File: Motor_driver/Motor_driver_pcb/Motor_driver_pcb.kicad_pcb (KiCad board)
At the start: 2 copper layers, 89 parts, among them J1 USB_B, J10 Stepper AB, J11 Uni_stepper, J2 Power, J3 Servo 1, J4 Servo 2, J5 Encoder 1, J6 Encoder 2, J7 Stepper CD, J8 Motor 1, J9 Motor 2, Q1 Q_NPN_EBC, Q10 IRF9540N, Q11 IRF540N, Q12 Q_NPN_EBC, Q13 Q_NPN_EBC, Q14 IRF9540N, Q15 IRF540N, Q16 IRF9540N, Q17 IRF540N, Q18 Q_NPN_EBC, Q19 Q_NPN_EBC, Q2 IRF9540N, Q20 IRF9540N, Q21 IRF540N, Q22 IRF9540N, Q23 IRF540N, Q24 Q_NPN_EBC, Q3 IRF540N, Q4 IRF9540N, Q5 IRF540N, Q6 Q_NPN_EBC, Q7 Q_NPN_EBC, Q8 IRF9540N, Q9 IRF540N, U1 LM2596S_Module, U2 FT232RL, U3 STM32F103C8T6, U4 CD40106BE, U5 CD40106BE

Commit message: finish schema and PCB update uC configuration
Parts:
- added C1: 10n, Capacitor_SMD:C_0805_2012Metric_Pad1.15x1.40mm_HandSolder, F.Cu at (65.5, 83.3)
- added C2: 4.7u, Capacitor_THT:CP_Radial_D5.0mm_P2.00mm, F.Cu at (74.9, 81.3)
- added REF**: MountingHole_3.2mm_M3_ISO7380_Pad, MountingHole:MountingHole_3.2mm_M3_ISO7380_Pad, F.Cu at (46.7, 110.5)
- added REF**: MountingHole_3.2mm_M3_ISO7380_Pad, MountingHole:MountingHole_3.2mm_M3_ISO7380_Pad, F.Cu at (168.9, 110.7)
- added REF**: MountingHole_3.2mm_M3_ISO7380_Pad, MountingHole:MountingHole_3.2mm_M3_ISO7380_Pad, F.Cu at (46.7, 16.3)
- added REF**: MountingHole_3.2mm_M3_ISO7380_Pad, MountingHole:MountingHole_3.2mm_M3_ISO7380_Pad, F.Cu at (169.2, 16.3)
- moved J6 161.5 mm to (50.5, 34.0)
- moved J5 153.3 mm to (50.5, 49.5), turned to 0 degrees
- moved R15 62.5 mm to (132.0, 62.2), turned to 270 degrees
- moved R16 59.0 mm to (132.0, 66.0), turned to 270 degrees
- moved Q12 58.6 mm to (128.1, 69.6), turned to 90 degrees
- moved R9 56.2 mm to (132.0, 48.9), turned to 270 degrees
- moved R13 56.2 mm to (135.1, 62.2), turned to 270 degrees
- moved JP1 54.2 mm to (120.1, 93.0)
- moved R1 54.0 mm to (132.1, 18.8), turned to 270 degrees
- moved R3 51.6 mm to (135.1, 18.8), turned to 270 degrees
- moved R2 48.2 mm to (132.1, 22.9), turned to 270 degrees
- moved Q11 47.9 mm to (149.7, 68.3)
- moved J9 46.7 mm to (166.2, 57.5)
- moved R7 46.0 mm to (132.1, 32.5), turned to 270 degrees
- moved R20 45.7 mm to (169.9, 92.5), turned to 90 degrees
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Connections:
- net Net-(J3-Pad3) renamed SERVO2
- net Net-(J4-Pad3) renamed SERVO1
- D11 pad 1: HV -> /sheet5CA1B149/HV
- D13 pad 1: HV -> /sheet5CA1B149/HV
- D15 pad 1: HV -> /sheet5CA1B149/HV
- D9 pad 1: HV -> /sheet5CA1B149/HV
- J11 pad 3: Net-(J11-Pad3) -> GND
- JP1 pad 2: Net-(J11-Pad3) -> /sheet5CA1B149/HV
- Q14 pad 3: HV -> /sheet5CA1B149/HV
- Q16 pad 3: HV -> /sheet5CA1B149/HV
- Q20 pad 3: HV -> /sheet5CA1B149/HV
- Q22 pad 3: HV -> /sheet5CA1B149/HV
- R17 pad 1: HV -> /sheet5CA1B149/HV
- R19 pad 1: HV -> /sheet5CA1B149/HV
- R21 pad 1: HV -> /sheet5CA1B149/HV
- R23 pad 1: HV -> /sheet5CA1B149/HV
- R25 pad 1: HV -> /sheet5CA1B149/HV
- R27 pad 1: HV -> /sheet5CA1B149/HV
- R29 pad 1: HV -> /sheet5CA1B149/HV
- R31 pad 1: HV -> /sheet5CA1B149/HV
- U3 pad 13: Net-(U2-Pad1) -> Net-(U3-Pad13)
- U3 pad 14: Net-(U2-Pad5) -> Net-(U3-Pad14)
- U3 pad 5: Net-(U3-Pad5) -> Net-(U2-Pad1)
- U3 pad 6: Net-(U3-Pad6) -> Net-(U2-Pad5)
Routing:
- net HV: track 0.00 -> 318.9 mm, vias 0 -> 2
- net 5V: track 0.00 -> 273.1 mm, vias 0 -> 4
- net /sheet5CA1B149/HV: track 0.00 -> 167.8 mm
- net /sheet5CA227AD/PWM_2: track 0.00 -> 105.9 mm
- net /sheet5CA1B149/PWM_2: track 0.00 -> 89.1 mm
- net /sheet5CA227AD/PWM_1: track 0.00 -> 81.7 mm
- net /sheet5CA1B149/PWM_1: track 0.00 -> 70.9 mm
- net /sheet5CA1B149/Motor_-: track 0.00 -> 70.2 mm
- net Net-(U3-Pad36): track 0.00 -> 63.1 mm
- net /sheet5CA227AD/Motor_+: track 0.00 -> 60.6 mm
- net ENC2A: track 0.00 -> 59.1 mm, vias 0 -> 1
- net /sheet5CA1B149/Motor_+: track 0.00 -> 58.3 mm
- net ENC2B: track 0.00 -> 56.7 mm, vias 0 -> 1
- net Net-(U3-Pad35): track 0.00 -> 56.0 mm
- net /sheet5CA227AD/Motor_-: track 0.00 -> 55.7 mm
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- added copper zone on B.Cu, net GND
- added copper zone on F.Cu, net GND
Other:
- board outline added: 129.5 x 101.6 mm
- board text added: "+ -"
- board text added: "- +"
- board text added: "Encoder 1"
- board text added: "Encoder 2"
- board text added: "In + -"
- board text added: "Motor 1"
- board text added: "Motor 2"
- board text added: "Servo 1"
- board text added: "Servo 2"
- board text added: "Universal DC Motor Driver v1.0 author: Kamil Kasjan"

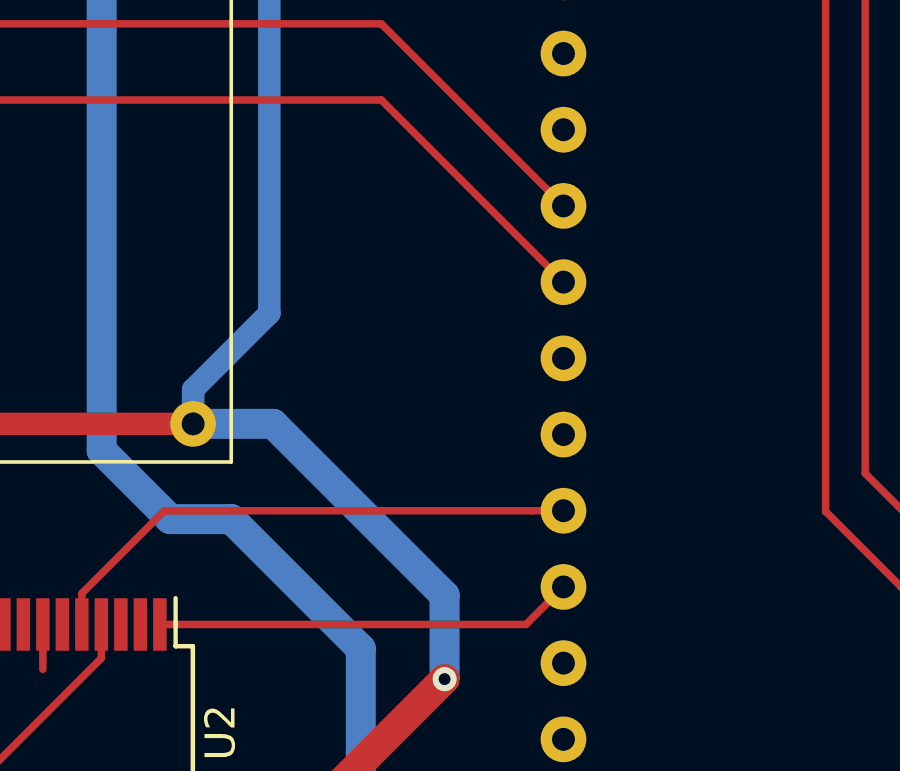
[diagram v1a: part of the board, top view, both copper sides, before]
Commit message: add BT_module PCB add Gerbera files
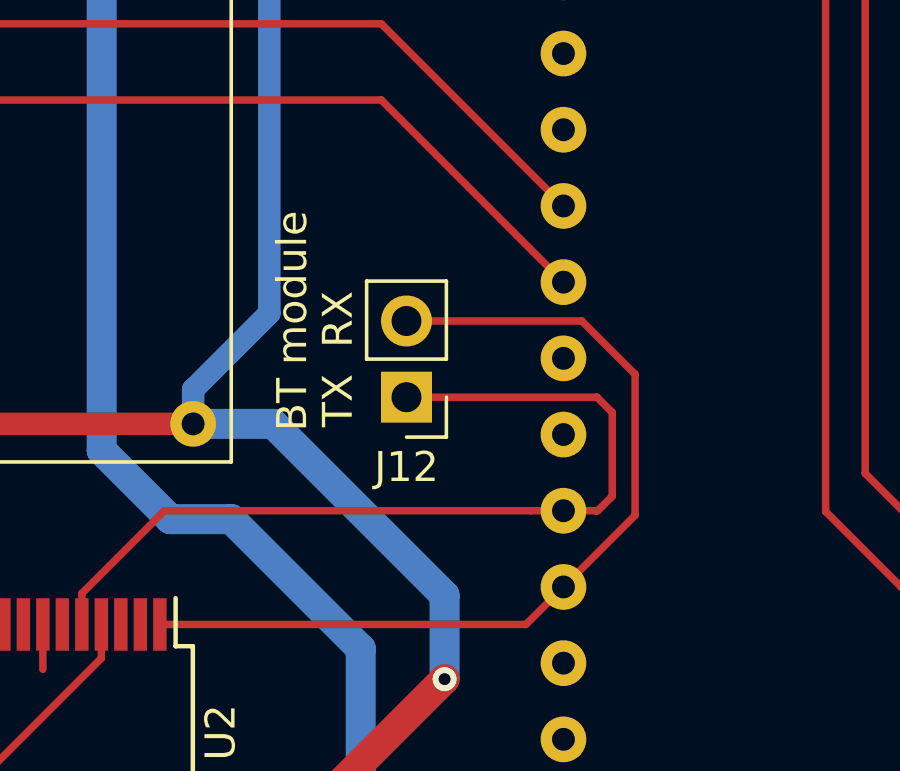
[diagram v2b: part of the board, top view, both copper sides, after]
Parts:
- added J12: BT_module, Connector_PinHeader_2.54mm:PinHeader_1x02_P2.54mm_Vertical, F.Cu at (83.1, 62.0)
- Q1, Q12, Q13, Q18, Q19, Q24, Q6, Q7: value Q_NPN_EBC -> 2N2222
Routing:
- net Net-(J12-Pad2): track 14.0 -> 30.4 mm
- net Net-(J12-Pad1): track 18.2 -> 29.9 mm
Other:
- board text added: "BT module"
- board text added: "TX RX"
